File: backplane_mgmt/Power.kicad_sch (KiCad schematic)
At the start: 63 parts, among them J304 VIn, Q301 SUD19P06-60, Q302 SUD19P06-60, U301 LDL1117S50R, U302 PTH08T220, U303 INA260, U304 INA260, U305 AT30TS74

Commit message: Minor tweaks to all boards
- Moved around some traces on the 68000 CPU card for prettiness

- Added a connector on the backplane to provide +5V/+12V without a
  management card installed (for testing)
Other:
- company: (none) -> Tristan Seifert
- title: (none) -> Backplane Management and Power
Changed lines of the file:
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@@
   (paper "A4")
   (title_block
+    (title "Backplane Management and Power")
+    (date "2022-01-09")
+    (rev "1")
+    (company "Tristan Seifert")
     (comment 1 "+5V caps must be 10V, +VIn/+12V 20V")
   )

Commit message: Tweaks to bill of materials
- Added missing MPN's for a few components; tweaked a few bits of layout
  to increase some tolerances

  This includes kind of tweaking the boot rom socket positions in hopes
  of fitting fancier sockets
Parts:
- C304: MPN (none) -> TAJA106K016RNJV
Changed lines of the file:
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@@
+      (effects (font (size 1.27 1.27)) hide)
+    )
+    (property "MPN" "TAJA106K016RNJV" (id 4) (at 73.025 182.245 0)
       (effects (font (size 1.27 1.27)) hide)
     )

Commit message: Tweaks to backplane management board
- Added pull downs to the audio inputs, so that if the backplane doesn't
  provide audio, the op amp inputs aren't floating

- Minor tweaks to some of the routing. Also switched out the 5V
  regulator for a larger, easier to get version, and added some large
  planes for power dissapation.
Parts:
- F301: value 140mA -> 100mA; MPN 0ZCG0014FF2C -> PTS181230V010
- R305: value 100k -> 1M
- U301: value LDL1117S50R -> AZ1117CD-5.0; footprint Package_TO_SOT_SMD:SOT-223-3_TabPin2 -> Package_TO_SOT_SMD:TO-252-2
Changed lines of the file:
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@@
     (in_bom yes) (on_board yes)
     (property "Reference" "F301" (id 0) (at 26.035 174.8495 90))
-    (property "Value" "140mA" (id 1) (at 26.035 177.6246 90))
+    (property "Value" "100mA" (id 1) (at 26.035 177.6246 90))
     (property "Footprint" "Fuse:Fuse_1812_4532Metric" (id 2) (at 31.115 178.435 0)
       (effects (font (size 1.27 1.27)) (justify left) hide)
@@
       (effects (font (size 1.27 1.27)) hide)
     )
-    (property "MPN" "0ZCG0014FF2C" (id 4) (at 26.035 179.705 90)
+    (property "MPN" "PTS181230V010" (id 4) (at 26.035 179.705 90)
       (effects (font (size 1.27 1.27)) hide)
     )
@@
   (symbol (lib_id "Regulator_Linear:LD1117S50TR_SOT223") (at 53.34 179.705 0) (unit 1)
     (in_bom yes) (on_board yes) (fields_autoplaced)
-    (property "Reference" "U301" (id 0) (at 53.34 173.8334 0))
-    (property "Value" "LDL1117S50R" (id 1) (at 53.34 176.6085 0))
-    (property "Footprint" "Package_TO_SOT_SMD:SOT-223-3_TabPin2" (id 2) (at 53.34 174.625 0)
+    (property "Reference" "U301" (id 0) (at 53.34 173.8335 0))
+    (property "Value" "AZ1117CD-5.0" (id 1) (at 53.34 176.6086 0))
+    (property "Footprint" "Package_TO_SOT_SMD:TO-252-2" (id 2) (at 53.34 174.625 0)
       (effects (font (size 1.27 1.27)) hide)
     )
@@
   (symbol (lib_id "Device:R_Small") (at 52.07 36.83 0) (mirror y) (unit 1)
     (in_bom yes) (on_board yes) (fields_autoplaced)
-    (property "Reference" "R305" (id 0) (at 54.61 35.5599 0)
-      (effects (font (size 1.27 1.27)) (justify right))
-    )
-    (property "Value" "100k" (id 1) (at 54.61 38.0999 0)
-      (effects (font (size 1.27 1.27)) (justify right))
-    )
+    (property "Reference" "R305" (id 0) (at 53.5686 35.9215 0)
+      (effects (font (size 1.27 1.27)) (justify right))
+    )
+    (property "Value" "1M" (id 1) (at 53.5686 38.6966 0)
+      (effects (font (size 1.27 1.27)) (justify right))
+    )

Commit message: Minor tweaks to power board
- Reorganized the layout of input protection to accomodate a different
  (cheaper) input connector; also added some better thermal dissipation
  for the protection MOSFETs.
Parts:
- J304: footprint Connector_Phoenix_MSTB:PhoenixContact_MSTBA_2,5_2-G-5,08_1x02_P5.08mm_Horizontal -> 68komputer-common:CUI_TBP01R1W-508-02BE; MPN 1748167 -> TBP01R1W-508-02BE; MPN2 1975079 -> TBP01P1W-508-02BE
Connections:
- net VIn: now also J304.1 (Pin_1); no longer J304.2 (Pin_2)
- net at L301.1: now also J304.2 (Pin_2); no longer J304.1 (Pin_1)
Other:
- moved on the sheet: J304
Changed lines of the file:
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@@
     (pin "1")
   )
-  (symbol (lib_id "Connector:Screw_Terminal_01x02") (at 24.765 29.21 180) (unit 1)
+  (symbol (lib_id "Connector:Screw_Terminal_01x02") (at 24.765 26.67 0) (mirror y) (unit 1)
     (in_bom yes) (on_board yes) (fields_autoplaced)
-    (property "Reference" "J304" (id 0) (at 24.765 19.685 0))
-    (property "Value" "VIn" (id 1) (at 24.765 22.225 0))
-    (property "Footprint" "Connector_Phoenix_MSTB:PhoenixContact_MSTBA_2,5_2-G-5,08_1x02_P5.08mm_Horizontal" (id 2) (at 24.765 29.21 0)
+    (property "Reference" "J304" (id 0) (at 24.765 21.4335 0))
+    (property "Value" "VIn" (id 1) (at 24.765 24.2086 0))
+    (property "Footprint" "68komputer-common:CUI_TBP01R1W-508-02BE" (id 2) (at 24.765 26.67 0)
       (effects (font (size 1.27 1.27)) hide)
     )
-    (property "Datasheet" "~" (id 3) (at 24.765 29.21 0)
+    (property "Datasheet" "~" (id 3) (at 24.765 26.67 0)
       (effects (font (size 1.27 1.27)) hide)
     )
-    (property "MPN" "1748167" (id 4) (at 24.765 29.21 0)
+    (property "MPN" "TBP01R1W-508-02BE" (id 4) (at 24.765 26.67 0)
       (effects (font (size 1.27 1.27)) hide)
     )
-    (property "MPN2" "1975079" (id 5) (at 24.765 29.21 0)
+    (property "MPN2" "TBP01P1W-508-02BE" (id 5) (at 24.765 26.67 0)
       (effects (font (size 1.27 1.27)) hide)
     )

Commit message: Added +12V regulator to backplane mgmt
- Added the components for a discrete switching regulator (that is, with
  external switching MOSFETs, but a fancy little switching controller)
  to generate the 12V rail, at up to 10A. This is then further regulated
  to provide 5V for the board itself, and for the rest of the system.
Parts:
- removed C312, C323, C324: 330µF, Capacitor_THT:CP_Radial_D8.0mm_P3.50mm, symbol Device:C_Polarized_Small
- added C312, C323, C324, C335, C336: 2.2µF, Capacitor_SMD:C_1206_3216Metric, symbol Device:C_Small
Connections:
- net GND: now also C312.2, C323.2, C324.2, C335.2, C336.2
- net VBUS: now also C312.1, C323.1, C324.1, C335.1, C336.1; no longer C310.1, C311.1, C318.1, C319.1, C320.1, C321.1, C325.1, F301.1, U302.10 (TRACK), U302.2 (VIN), U304.1 (IN+), U304.12 (VBUS), U304.2 (IN+), U304.3 (IN+)
- new net VDD: C310.1, C311.1, C318.1, C319.1, C320.1, C321.1, C325.1, F301.1, U302.10 (TRACK), U302.2 (VIN), U304.1 (IN+), U304.12 (VBUS), U304.2 (IN+), U304.3 (IN+)
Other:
- added sheet 12V boi (vreg-12v.kicad_sch)
- note added: "+12V Current Sense"
- note removed: "+12V Conditioning (from VIn)"
- moved on the sheet: C313, C314

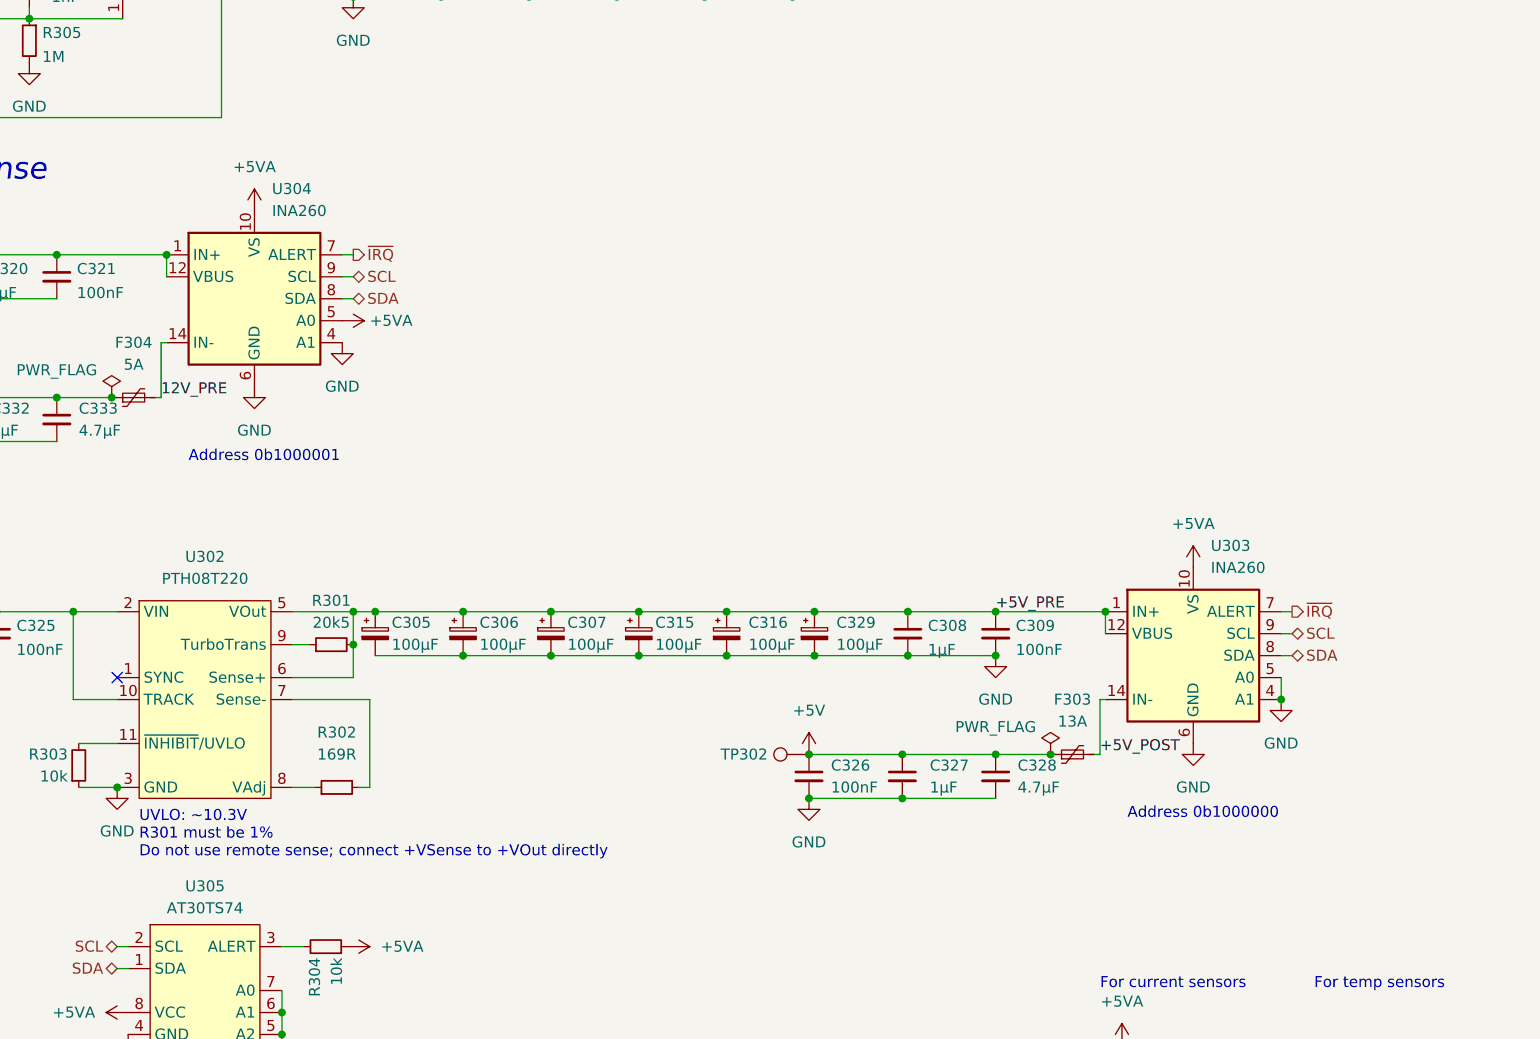
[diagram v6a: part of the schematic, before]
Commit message: Replaced current sense with shunt+INA209
- Instead of using unobtanium parts for the current sensing, we're
  instead just gonna use more of the shunt we already have to get for
  the current limit of the switching regulator, and then measuring the
  voltage drop with the INA209 which is functionally going to give us
  the same exact behavior as before.
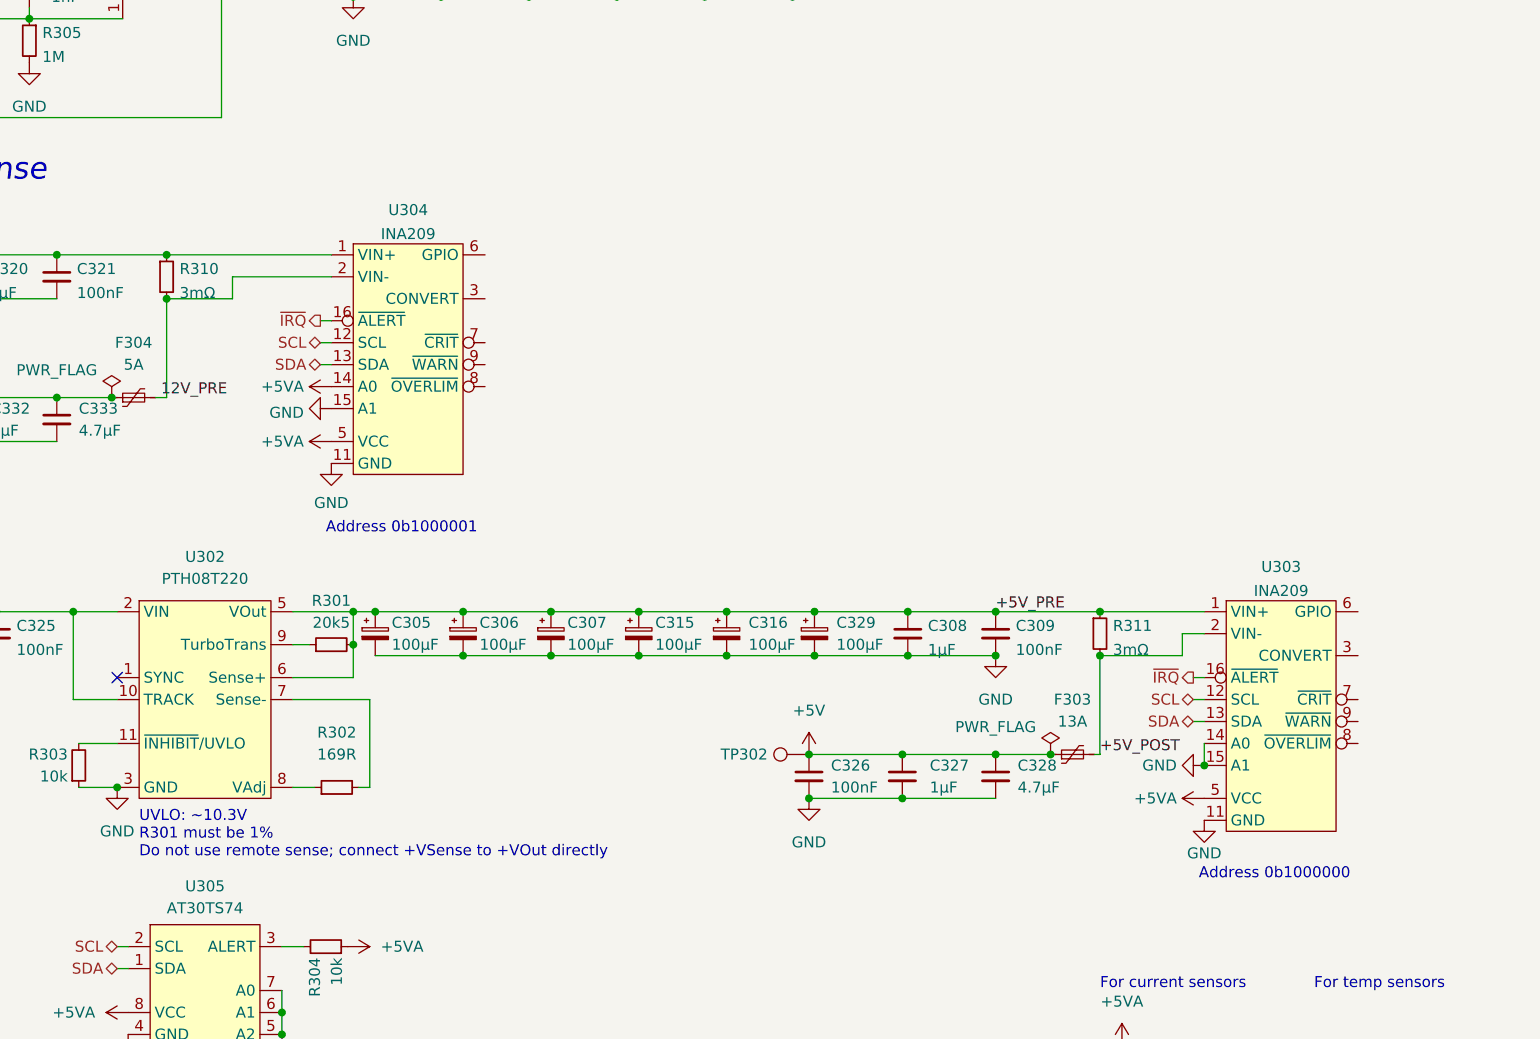
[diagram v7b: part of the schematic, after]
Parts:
- removed U303, U304: INA260, Package_SO:TSSOP-16_4.4x5mm_P0.65mm, symbol Sensor:INA260
- added R310, R311: 3mΩ, Resistor_SMD:R_2512_6332Metric_Pad1.40x3.35mm_HandSolder, symbol Device:R_Small
- added U303, U304: INA209, Package_SO:TSSOP-16_4.4x5mm_P0.65mm, symbol 68komputer-common:INA209
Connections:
- net +5VA: now also U303.10 (VCC), U303.5 (VCC), U304.10 (VCC), U304.14 (A0), U304.5 (VCC)
- net +5V_POST: now also R311.2, U303.2 (VIN-)
- net +5V_PRE: now also R311.1, U303.1 (VIN+)
- net 12V_PRE: now also R310.2, U304.2 (VIN-)
- net GND: now also U303.11 (GND), U303.14 (A0), U303.15 (A1), U303.4 (GND), U304.11 (GND), U304.15 (A1), U304.4 (GND)
- net SCL: now also U303.12 (SCL), U304.12 (SCL)
- net SDA: now also U303.13 (SDA), U304.13 (SDA)
- net VDD: now also R310.1, U304.1 (VIN+)
- net ~{IRQ}: now also U303.16 (~{ALERT}), U304.16 (~{ALERT})
